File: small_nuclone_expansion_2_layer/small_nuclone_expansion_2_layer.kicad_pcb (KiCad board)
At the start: 2 copper layers, 50 x 50 mm, 26 parts, among them J3 nuclone_small_left, J4 nuclone_small_right

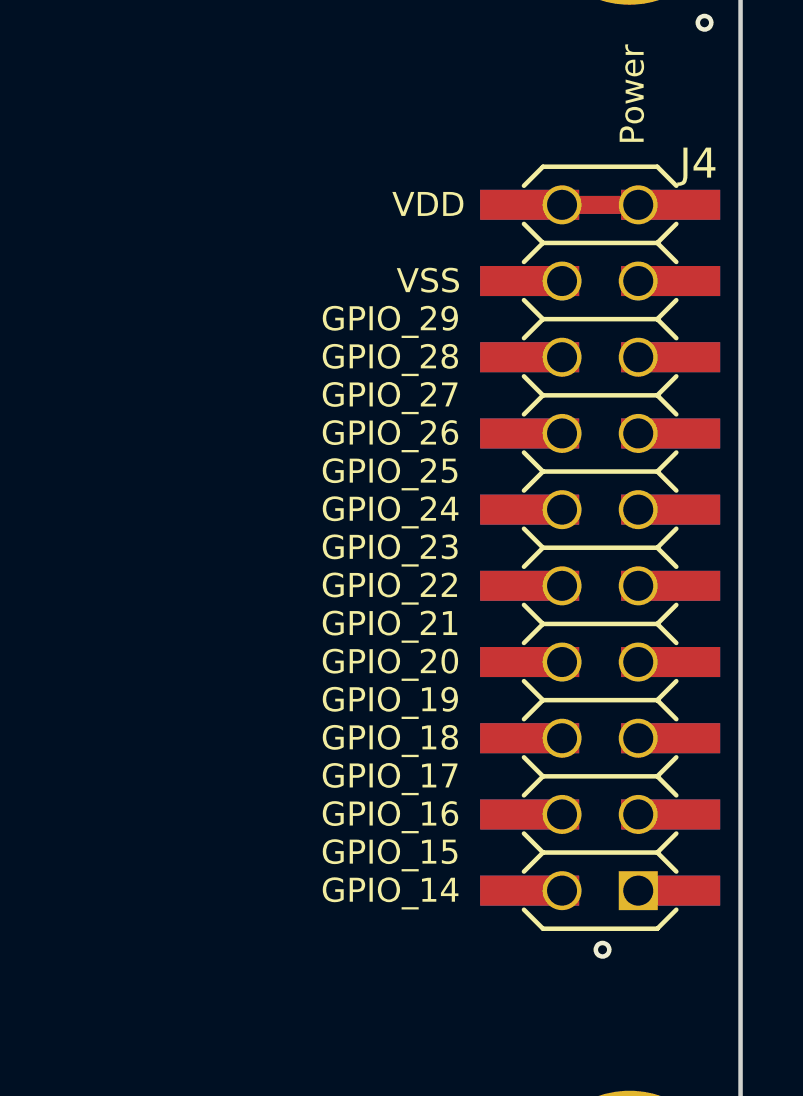
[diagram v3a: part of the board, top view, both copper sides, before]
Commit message: added left side connector test points
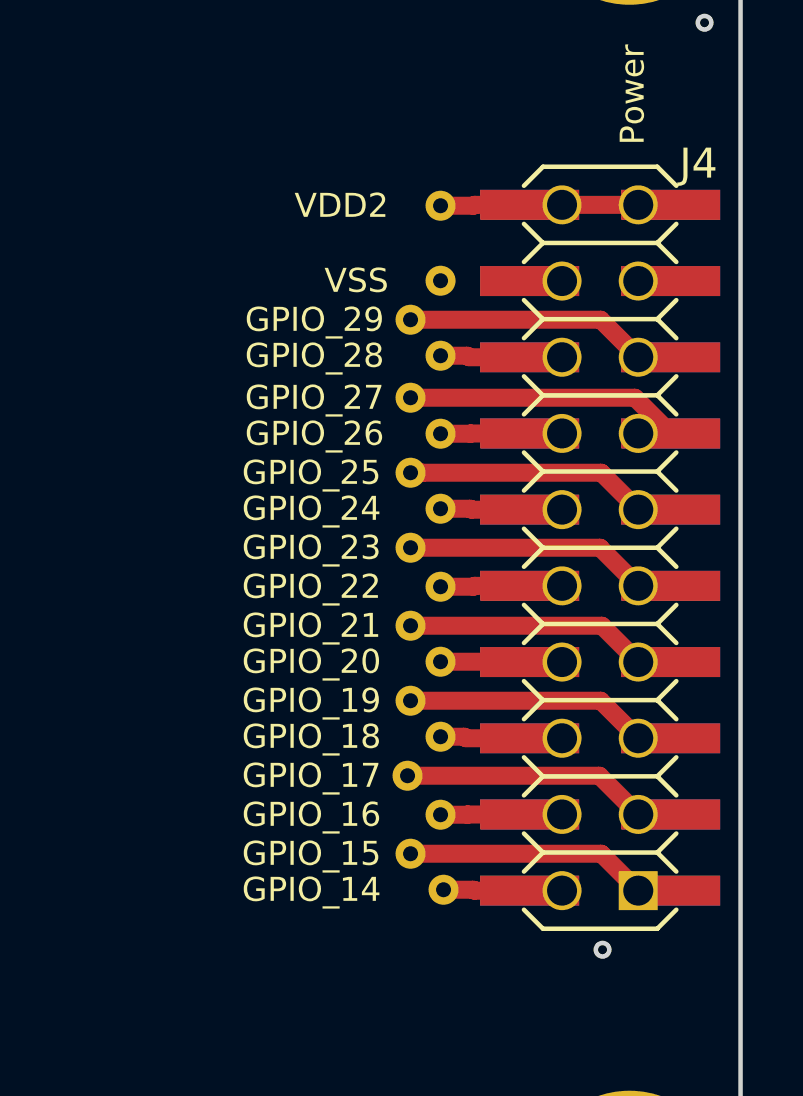
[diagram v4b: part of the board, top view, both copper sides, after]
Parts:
- added TP18: VDD2, SquantorTestPoints:TestPoint_hole_H05R10_small_text, F.Cu at (100.0, 74.6)
- added TP19: VSS, SquantorTestPoints:TestPoint_hole_H05R10_small_text, F.Cu at (100.0, 77.1)
- added TP20: GPIO_29, SquantorTestPoints:TestPoint_hole_H05R10_small_text, F.Cu at (99.0, 78.4)
- added TP21: GPIO_28, SquantorTestPoints:TestPoint_hole_H05R10_small_text, F.Cu at (100.0, 79.6)
- added TP22: GPIO_27, SquantorTestPoints:TestPoint_hole_H05R10_small_text, F.Cu at (99.0, 81.0)
- added TP23: GPIO_26, SquantorTestPoints:TestPoint_hole_H05R10_small_text, F.Cu at (100.0, 82.2)
- added TP24: GPIO_25, SquantorTestPoints:TestPoint_hole_H05R10_small_text, F.Cu at (99.0, 83.5)
- added TP25: GPIO_24, SquantorTestPoints:TestPoint_hole_H05R10_small_text, F.Cu at (100.0, 84.7)
- added TP26: GPIO_23, SquantorTestPoints:TestPoint_hole_H05R10_small_text, F.Cu at (99.0, 86.0)
- added TP27: GPIO_22, SquantorTestPoints:TestPoint_hole_H05R10_small_text, F.Cu at (100.0, 87.3)
- added TP28: GPIO_21, SquantorTestPoints:TestPoint_hole_H05R10_small_text, F.Cu at (99.0, 88.6)
- added TP29: GPIO_20, SquantorTestPoints:TestPoint_hole_H05R10_small_text, F.Cu at (100.0, 89.8)
- added TP30: GPIO_19, SquantorTestPoints:TestPoint_hole_H05R10_small_text, F.Cu at (99.0, 91.1)
- added TP31: GPIO_18, SquantorTestPoints:TestPoint_hole_H05R10_small_text, F.Cu at (100.0, 92.3)
- added TP32: GPIO_17, SquantorTestPoints:TestPoint_hole_H05R10_small_text, F.Cu at (98.9, 93.6)
- added TP33: GPIO_16, SquantorTestPoints:TestPoint_hole_H05R10_small_text, F.Cu at (100.0, 94.9)
- added TP34: GPIO_15, SquantorTestPoints:TestPoint_hole_H05R10_small_text, F.Cu at (99.0, 96.2)
- added TP35: GPIO_14, SquantorTestPoints:TestPoint_hole_H05R10_small_text, F.Cu at (100.1, 97.4)
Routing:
- net /GPIO_27: track 0.00 -> 9.16 mm
- net /GPIO_25: track 0.00 -> 8.40 mm
- net /GPIO_17: track 0.00 -> 8.22 mm
- net /GPIO_23: track 0.00 -> 8.12 mm
- net /GPIO_29: track 0.00 -> 8.11 mm
- net /GPIO_19: track 0.00 -> 8.11 mm
- net /GPIO_15: track 0.00 -> 8.10 mm
- net /GPIO_21: track 0.00 -> 8.09 mm
- net /GPIO_28: track 0.00 -> 2.99 mm
- net /GPIO_18: track 0.00 -> 2.99 mm
- net /VDD2: track 4.70 -> 7.68 mm
- net /GPIO_24: track 0.00 -> 2.98 mm
- net /GPIO_22: track 0.00 -> 2.98 mm
- net /GPIO_16: track 0.00 -> 2.97 mm
- net /GPIO_26: track 0.00 -> 2.97 mm
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
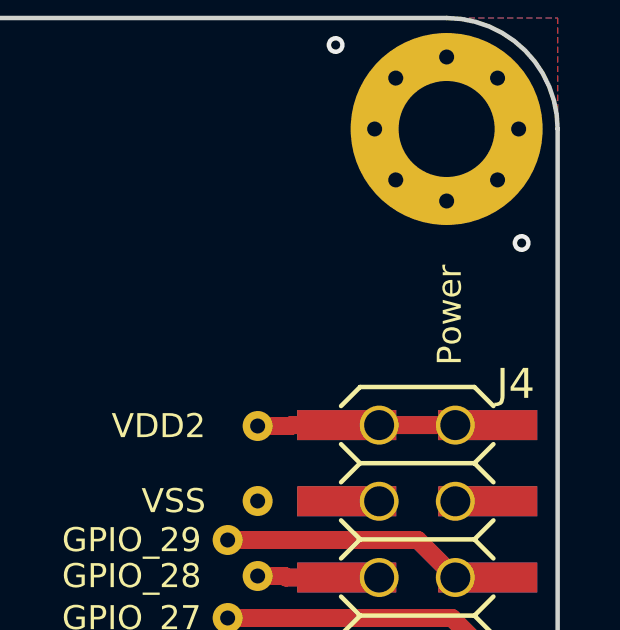
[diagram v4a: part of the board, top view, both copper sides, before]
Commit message: removed old label
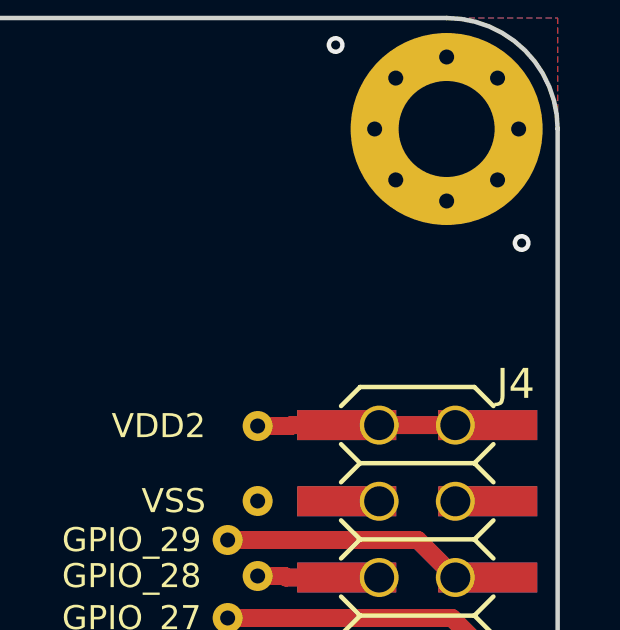
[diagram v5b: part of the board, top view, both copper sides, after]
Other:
- board text removed: "Power"
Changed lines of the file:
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@@
   (general
     (thickness 1.6)
-    (drawings 20)
+    (drawings 19)
     (tracks 98)
     (zones 0)
@@
   (gr_arc (start 106.3 107.3) (end 106.3 111) (angle -90) (layer Edge.Cuts) (width 0.15))
   (gr_arc (start 106.3 64.7) (end 110 64.7) (angle -90) (layer Edge.Cuts) (width 0.15))
-  (gr_text Power (at 106.4 70.9 90) (layer F.SilkS)
-    (effects (font (size 0.8 0.8) (thickness 0.12)))
-  )
   (gr_line (start 106.3 61) (end 63.7 61) (layer Edge.Cuts) (width 0.15))
   (gr_arc (start 63.7 64.7) (end 63.7 61) (angle -90) (layer Edge.Cuts) (width 0.15))

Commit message: added documentation block for the breakout of testpads
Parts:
- N2: value V20220215 -> V20220217

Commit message: conversion to kicad 6
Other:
- net class Default removed
- net class Power removed
- net class Signal removed

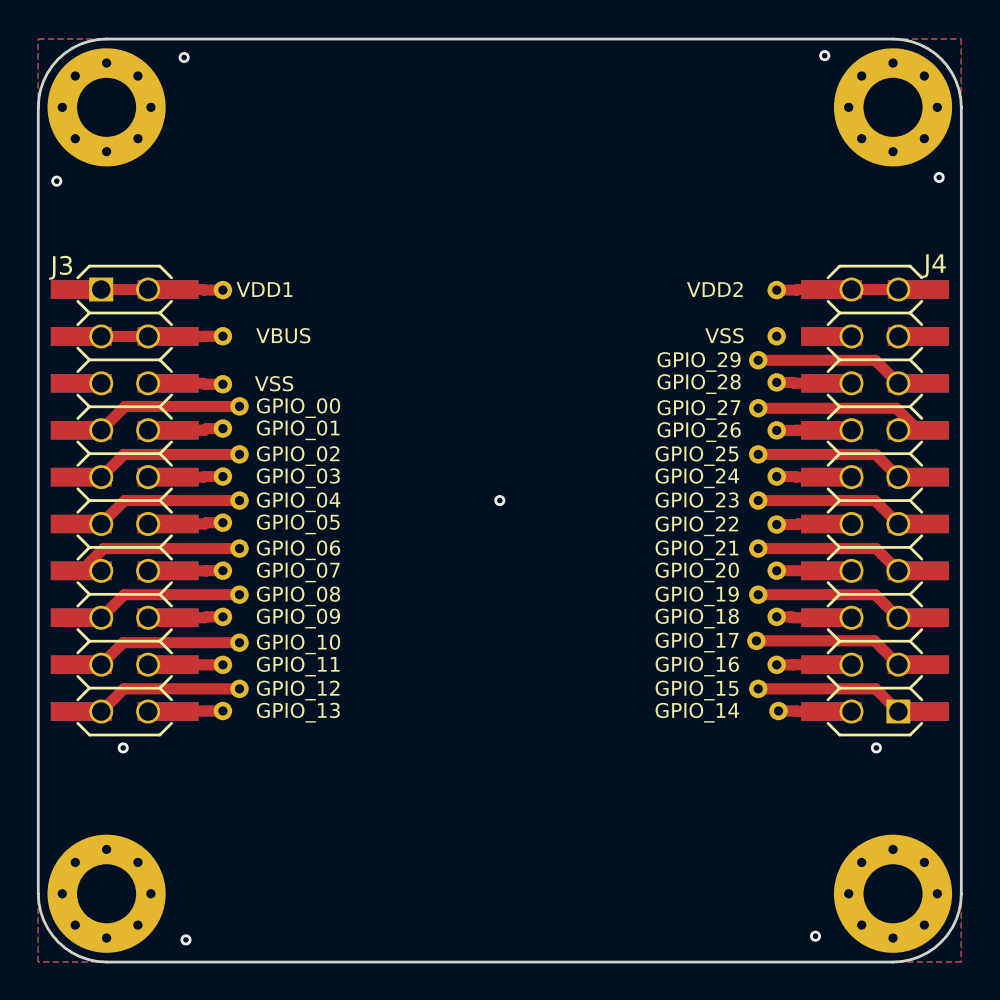
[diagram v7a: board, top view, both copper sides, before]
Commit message: prettyfied the small nuclone expansion
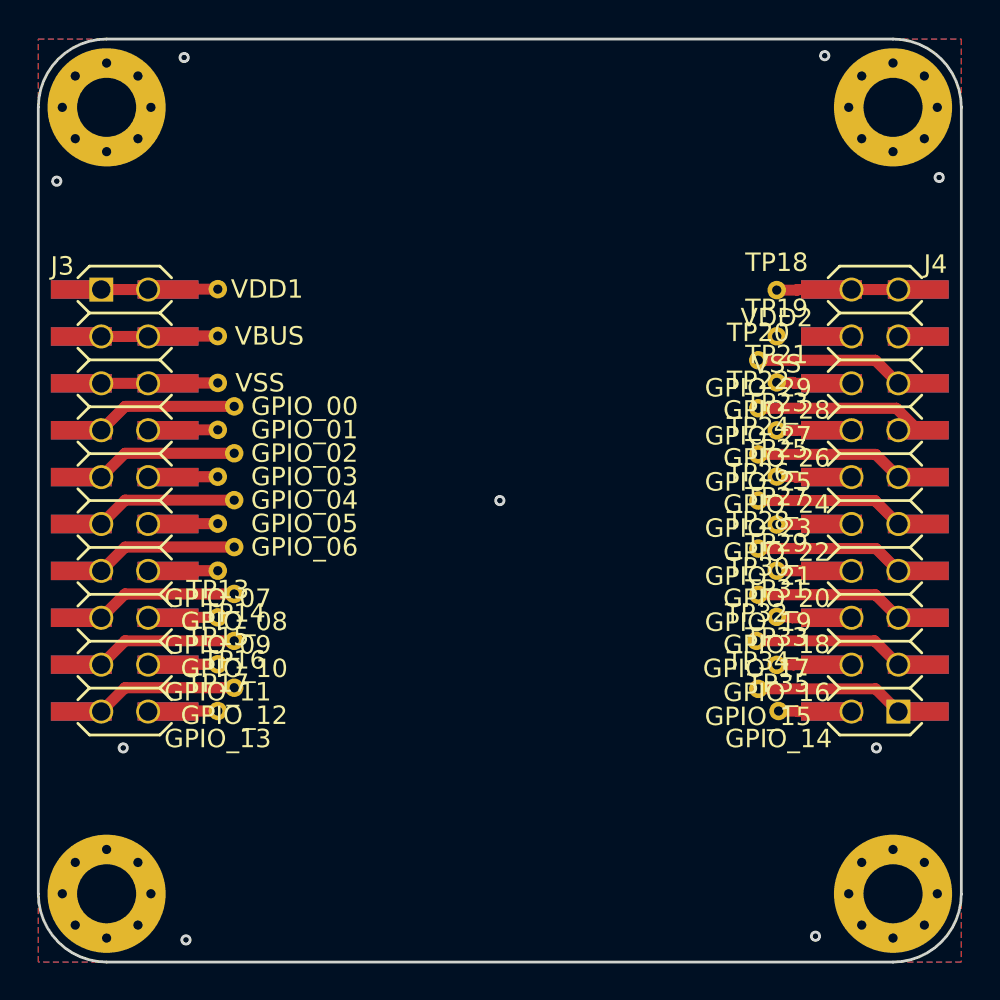
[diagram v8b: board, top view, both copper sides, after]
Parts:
- TP1, TP10, TP11, TP12, TP13, TP14, TP15, TP16, TP17, TP18, TP19, TP2, TP20, TP21, TP22, TP23, TP24, TP25, TP26, TP27, TP28, TP29, TP3, TP30, TP31, TP32, TP33, TP34, TP35, TP4, TP5, TP6, TP7, TP8, TP9: footprint SquantorTestPoints:TestPoint_hole_H05R10_small_text -> SquantorTestPoints:TestPoint_hole_H05R10_2side
- moved TP14 0.31 mm to (70.6, 93.6)
- moved TP10 0.30 mm to (70.6, 88.5)
- moved TP16 0.29 mm to (70.6, 96.1)
- moved TP6 0.29 mm to (70.6, 83.4)
- moved TP12 0.29 mm to (70.6, 91.1)
- moved TP8 0.29 mm to (70.6, 86.0)
- moved TP4 0.29 mm to (70.6, 80.9)
- moved TP3 0.29 mm to (69.7, 79.6)
- moved TP5 0.29 mm to (69.7, 82.2)
- moved TP1 0.28 mm to (69.7, 74.5)
- moved TP9 0.28 mm to (69.7, 87.2)
- moved TP15 0.28 mm to (69.7, 94.9)
- moved TP13 0.28 mm to (69.7, 92.3)
- moved TP2 0.28 mm to (69.7, 77.1)
- moved TP7 0.28 mm to (69.7, 84.7)
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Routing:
- net /VSS: track 2.99 -> 5.24 mm
- net /GPIO_06: track 9.07 -> 7.74 mm
